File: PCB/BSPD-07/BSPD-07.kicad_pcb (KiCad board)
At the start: 2 copper layers, 31.8 x 53.9 mm, 54 parts, among them IC1 LM393LVQDRQ1, IC2 LM393LVQDRQ1, IC3 LM393LVQDRQ1, IC4 LDO40LPU50RY, IC5 74LVC1G02GW-Q100H, J1 DTM13-12PA, Q1 RSQ025P03HZGTR, Q2 RJU002N06FRAT106, Q3 RJU002N06FRAT106, U2 TLP175A / COMUS AB38-Q

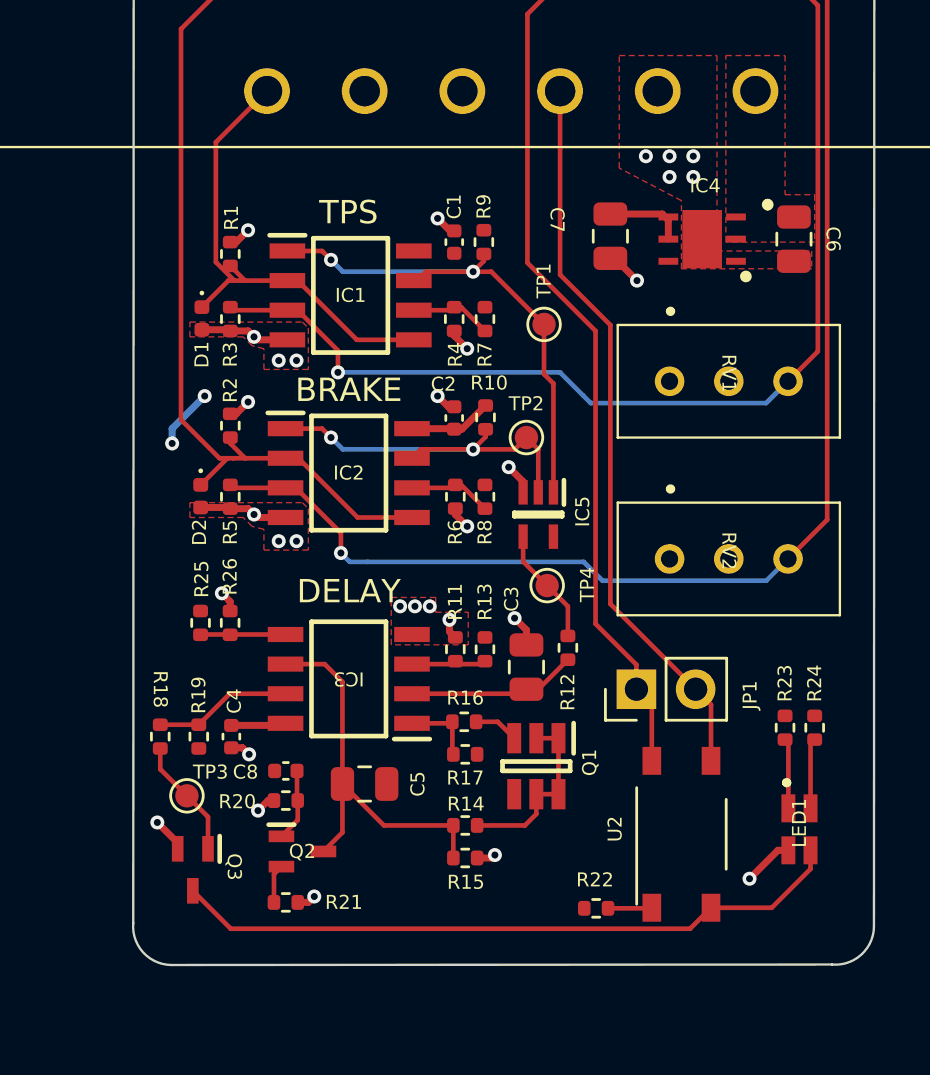
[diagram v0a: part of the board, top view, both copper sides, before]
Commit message: Initial silkscreen rework
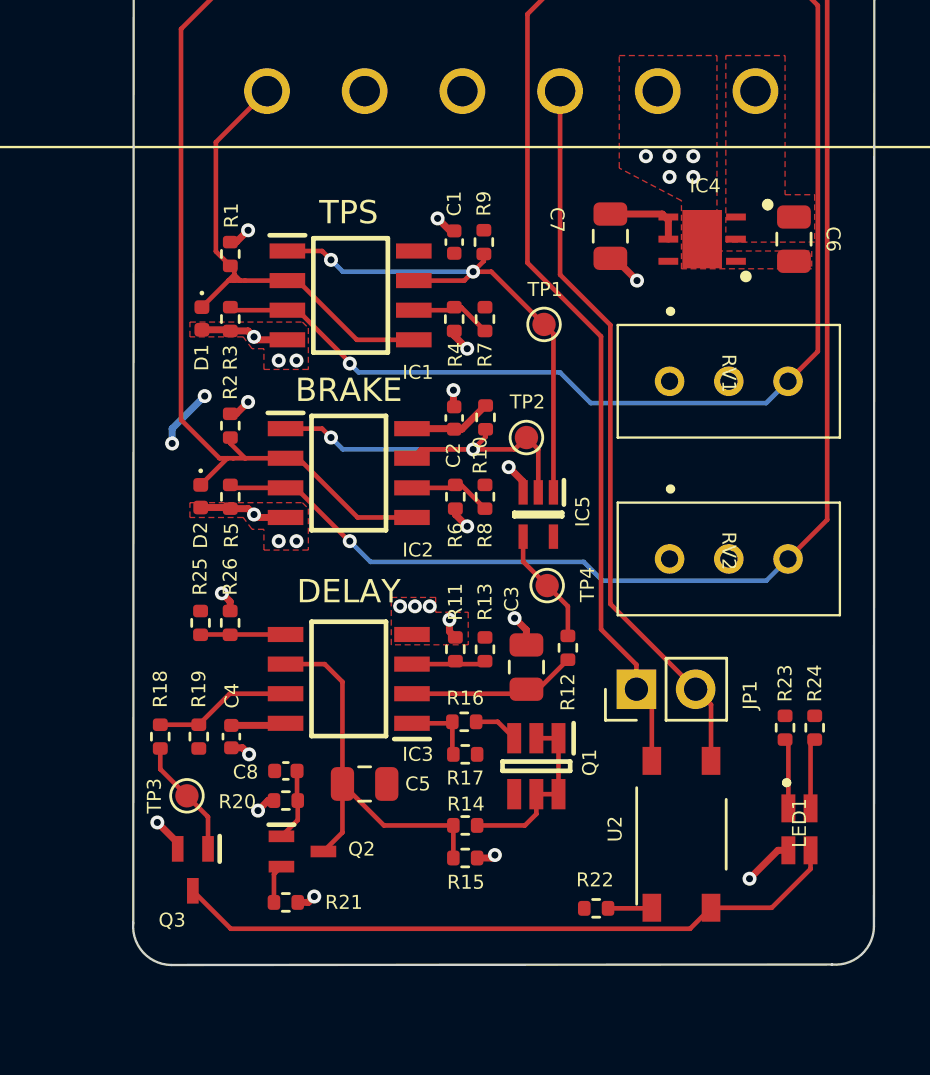
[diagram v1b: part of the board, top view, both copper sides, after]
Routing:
- net TPS_TRIG: track 47.0 -> 46.5 mm
- net BRAKE_TRIG: track 61.3 -> 60.8 mm

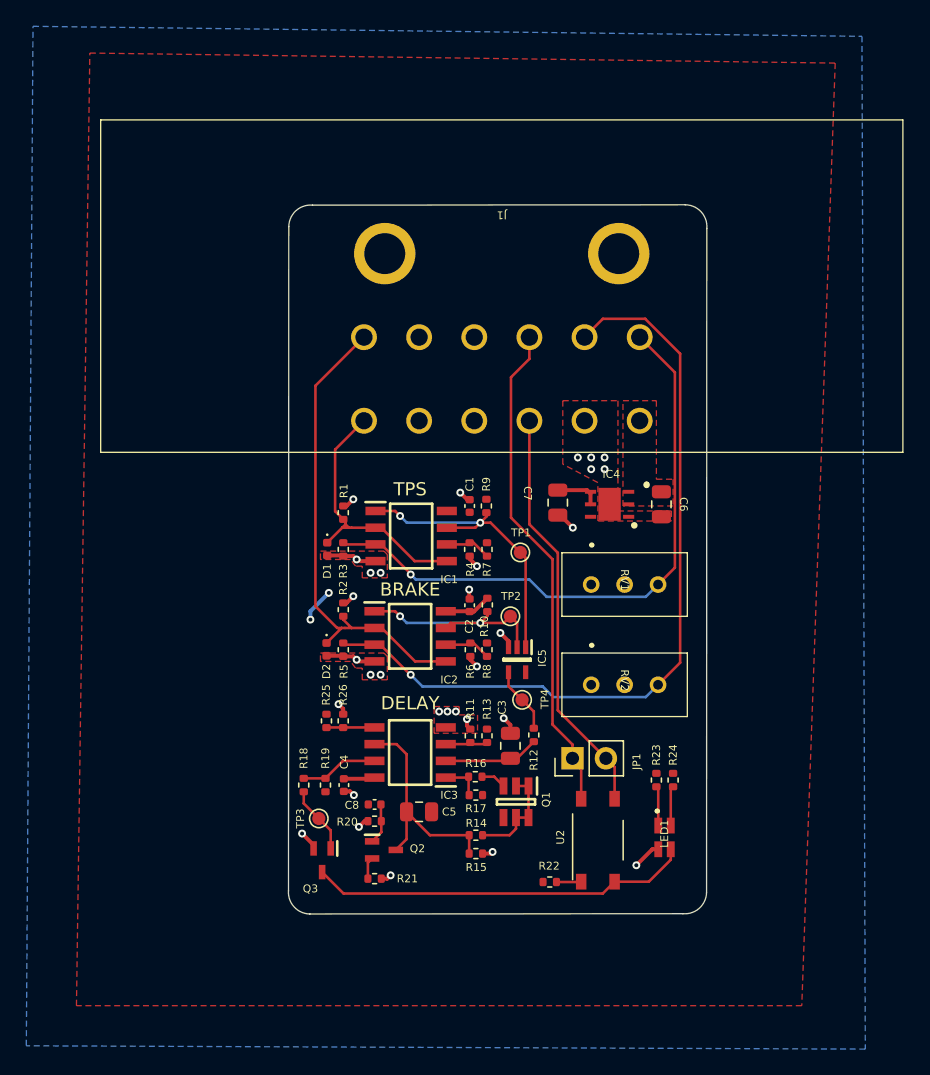
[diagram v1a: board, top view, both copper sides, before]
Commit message: Layout rework + led change
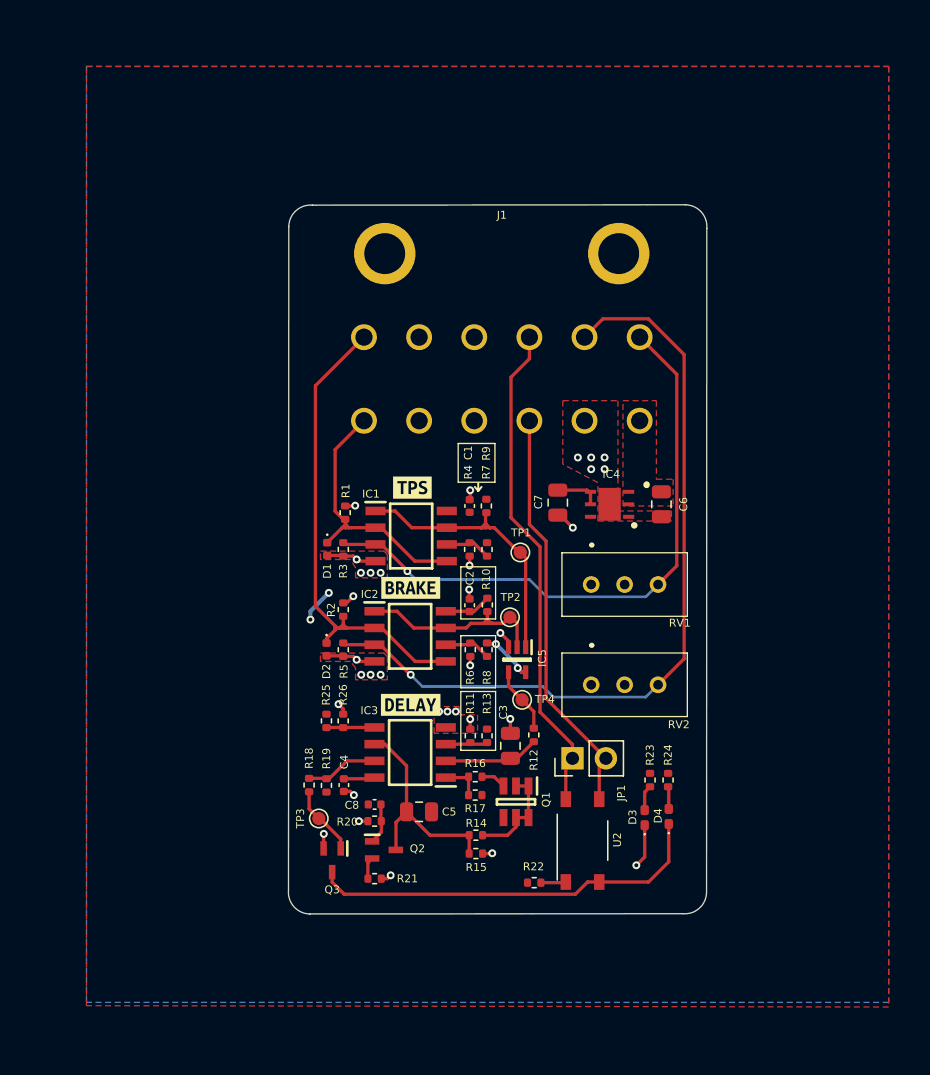
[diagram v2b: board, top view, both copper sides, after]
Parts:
- removed LED1: APHBM2012SURKCGKC, BSPD_07:APHBM2012SURKCGKC
- added D3: LED, Diode_SMD:D_0402_1005Metric_Pad0.77x0.64mm_HandSolder, F.Cu at (174.9, 129.0)
- added D4: LED, Diode_SMD:D_0402_1005Metric_Pad0.77x0.64mm_HandSolder, F.Cu at (176.7, 128.9)
- added kibuzzard-64754545: G***, kibuzzard-64754545, F.Cu at (157.1, 111.5)
- added kibuzzard-6475455D: G***, kibuzzard-6475455D, F.Cu at (157.2, 103.9)
- added kibuzzard-64754577: G***, kibuzzard-64754577, F.Cu at (157.1, 120.4)
- added kibuzzard-6475F124: G***, kibuzzard-6475F124, B.Cu at (152.1, 118.2)
- moved R22 1.18 mm to (166.5, 133.9)
- moved U2 1.17 mm to (170.1, 130.7)
- moved Q3 0.76 mm to (151.1, 132.2)
- moved R23 0.48 mm to (175.3, 126.1)
- moved R18 0.41 mm to (149.3, 126.5)
- moved R24 0.38 mm to (176.6, 126.1)
- moved R1 0.15 mm to (152.1, 105.8)
- moved TP2 0.08 mm to (164.6, 113.8)
- moved R19 0.08 mm to (150.7, 126.5)
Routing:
- net +5V: track 12.0 -> 15.9 mm, vias 2 -> 4
- net BRAKE_COMP_OUT: track 17.3 -> 15.4 mm, vias 2 -> 0
- net INFO_LED: track 29.0 -> 30.6 mm
- net TPS_COMP_OUT: track 23.3 -> 22.0 mm, vias 2 -> 0
- net Net-(R24-Pad1): track 3.02 -> 1.71 mm
- net Net-(R23-Pad1): track 3.01 -> 1.94 mm
- net GND: track 26.3 -> 25.4 mm, vias 31 -> 33
- net SAFETY_IN: track 37.9 -> 38.8 mm
- net BRAKE_IN: track 36.4 -> 37.0 mm
- net /10ms VAL: track 17.3 -> 16.7 mm
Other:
- board text removed: "BRAKE"
- board text removed: "BSPD - FSG 2023"
- board text removed: "DELAY"
- board text removed: "TPS"

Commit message: Reworked layout finished
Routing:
- net SAFETY_IN: track 38.8 -> 37.8 mm

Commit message: Revised layout
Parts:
- removed kibuzzard-64754545: G***, kibuzzard-64754545
- added Q4: AO3401A, Package_TO_SOT_SMD:SOT-23, F.Cu at (176.1, 102.9)
- added kibuzzard-647616BB: G***, kibuzzard-647616BB, F.Cu at (157.1, 111.5)
- moved JP1 3.01 mm to (170.0, 127.4)
- moved RV2 2.54 mm to (173.3, 121.4)
- moved RV1 2.44 mm to (173.2, 113.7)
- moved C6 2.42 mm to (177.0, 107.4)
- moved IC4 2.42 mm to (173.1, 107.4)
- moved C7 2.42 mm to (169.2, 107.3)
- moved R22 2.38 mm to (165.0, 132.1), turned to -90 degrees
- moved U2 2.03 mm to (170.0, 132.8), turned to 0 degrees
- moved D3 1.21 mm to (175.8, 129.7)
- moved D4 1.21 mm to (177.6, 129.6)
- moved R23 1.21 mm to (176.2, 126.9)
- moved R24 1.21 mm to (177.6, 126.9)
- moved J1 0.63 mm to (174.4, 98.2)
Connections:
- C6 pad 1: +12V -> Net-(C6-Pad1)
- IC4 pad 2: +12V -> Net-(C6-Pad1)
- IC4 pad 3: +12V -> Net-(C6-Pad1)
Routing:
- net SAFETY_OUT: track 31.4 -> 39.7 mm
- net SAFETY_IN: track 37.8 -> 44.2 mm
- net +12V: track 0.00 -> 4.44 mm
- net TPS_TRIG: track 46.6 -> 51.0 mm, vias 1 -> 2
- net GND: track 25.3 -> 22.5 mm, vias 33 -> 37
- net TPS_IN: track 20.9 -> 18.4 mm
- net BRAKE_TRIG: track 61.2 -> 62.5 mm
- net INFO_LED: track 30.6 -> 31.8 mm
- net BRAKE_IN: track 37.0 -> 37.6 mm
- added copper zone on F.Cu, net Net-(C6-Pad1)
- removed copper zone on F.Cu, net +12V
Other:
- board size 31.8 x 53.9 mm -> 31.5 x 53.5 mm
